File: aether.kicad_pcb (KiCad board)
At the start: 4 copper layers, 100.1 x 60.2 mm, 175 parts, among them J1 XT30PW-M, J2 Screw_Terminal_01x04, Q1 NPN, Q2 CSD17575Q3, Q3 CSD17575Q3, Q4 CSD17575Q3, Q5 CSD17575Q3, Q6 PNP, U1 USBLC6-2SC6, U10 TPS562201DDCR, U11 TPS562201DDCR, U12 INA219AxD, U2 USBLC6-2SC6, U3 SAM-M10Q-00B, U4 DPS310, U5 H3LIS331DL, U6 LSM6DSO32TR, U7 PCA9685PW, U8 MS860702BA01-50, U9 SHT45-AD1B-R2

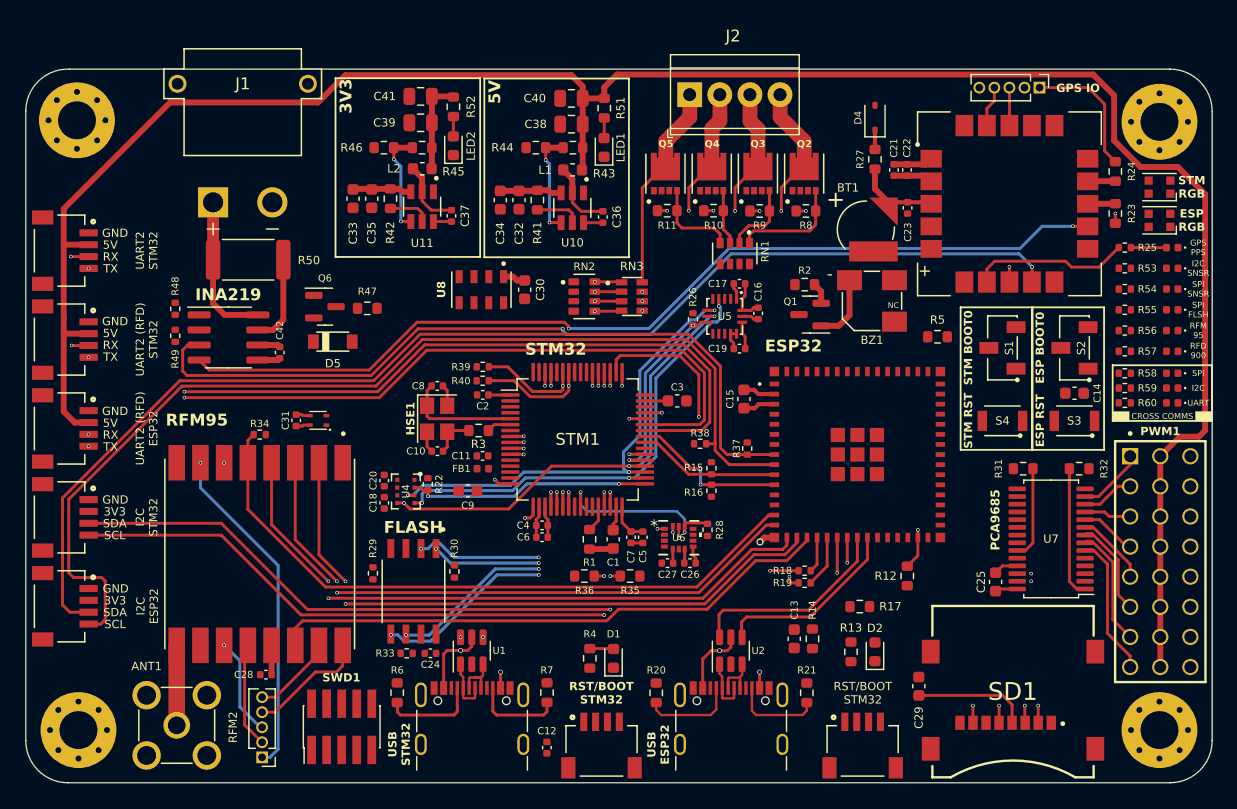
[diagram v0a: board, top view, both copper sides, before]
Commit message: signals routed
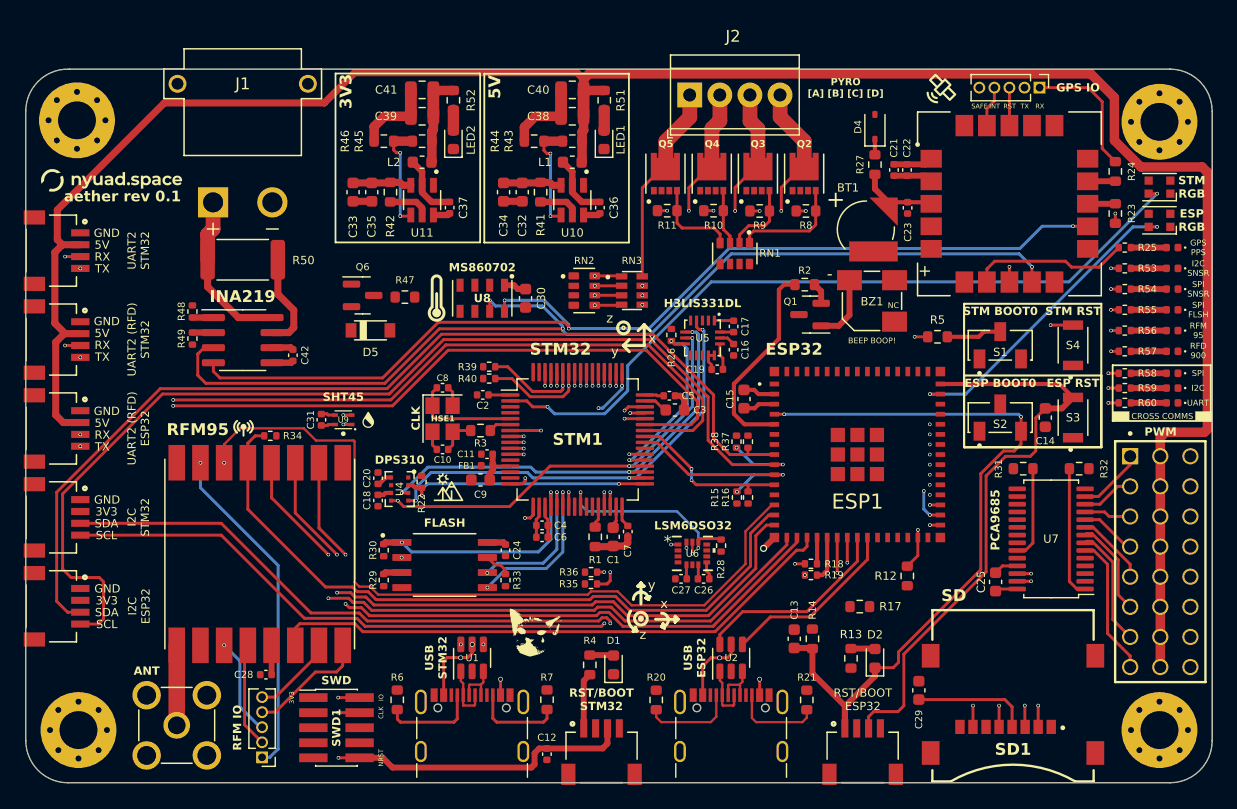
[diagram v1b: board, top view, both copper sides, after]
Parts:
- added G***: LOGO, LOGO, F.Cu at (133.9, 104.3)
- added G***: LOGO, LOGO, F.Cu at (116.6, 99.3)
- added G***: LOGO, LOGO, F.Cu at (127.1, 98.7)
- added G***: LOGO, LOGO, F.Cu at (141.0, 116.5)
- added G***: LOGO, LOGO, F.Cu at (175.5, 70.7)
- added G***: LOGO, LOGO, F.Cu at (105.4, 78.4)
- added G***: LOGO, LOGO, F.Cu at (132.9, 88.4)
- R35, R36: footprint Resistor_SMD:R_0603_1608Metric -> Resistor_SMD:R_0402_1005Metric
- moved C5 12.1 mm to (152.5, 96.6), turned to 0 degrees
- moved C24 10.8 mm to (138.7, 109.6), turned to -90 degrees
- moved R33 10.4 mm to (138.7, 112.2), turned to 90 degrees
- moved S4 8.72 mm to (186.6, 92.3), turned to 90 degrees
- moved S2 8.59 mm to (180.4, 98.4), turned to 0 degrees
- moved R30 6.23 mm to (128.4, 109.6)
- moved C16 3.70 mm to (157.9, 92.7), turned to -90 degrees
- moved C17 3.63 mm to (157.9, 90.8), turned to -90 degrees
- moved W25Q1 3.44 mm to (133.6, 110.9), turned to 0 degrees
- moved R35 3.36 mm to (145.9, 112.5), turned to 180 degrees
- moved D5 3.31 mm to (127.3, 91.1)
- moved Q6 3.31 mm to (126.7, 88.1)
- moved R47 3.31 mm to (130.2, 88.3)
- moved R15 3.27 mm to (158.2, 105.2), turned to -90 degrees
- moved C14 3.21 mm to (184.2, 98.4), turned to -90 degrees
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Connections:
- ESP1 pad 44: unconnected-(ESP1-IO46-Pad44) -> ESP32-RGB_IN
- RST-BOOT-ESP1 pad 2: GND -> 3.3V
- STM1 pad 2: unconnected-(STM1-PC13-Pad2) -> STM32-RGB_IN
- SWD1 pad 7: unconnected-(SWD1-Pin_7-Pad7) -> GND
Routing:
- net STM32-NRST: track 0.00 -> 119.3 mm, vias 0 -> 3
- net RFM95W_RST: track 0.00 -> 67.0 mm
- net STM32-RGB_IN: track 0.00 -> 64.7 mm, vias 0 -> 2
- net ESP32-GPIO0: track 0.05 -> 64.2 mm, vias 0 -> 2
- net GPS_SCL: track 94.8 -> 152.2 mm, vias 4 -> 6
- net GPS_SDA: track 95.1 -> 147.4 mm, vias 4 -> 6
- net ESP32-EN: track 0.01 -> 50.0 mm
- net STM32-BOOT0: track 0.02 -> 42.9 mm, vias 0 -> 2
- net STM32-SWCLK: track 1.15 -> 42.1 mm, vias 1 -> 3
- net STM32-SWDIO: track 0.00 -> 39.7 mm, vias 0 -> 2
- net ESP32-SPI2_MOSI: track 0.00 -> 37.7 mm, vias 0 -> 2
- net ESP32-SPI2_SCK: track 0.00 -> 36.5 mm, vias 0 -> 3
- net ESP32-SPI2_MISO: track 0.00 -> 35.8 mm, vias 0 -> 2
- net ESP32-RGB_IN: track 0.00 -> 26.6 mm, vias 0 -> 2
- net I2C-1_STM32: track 0.00 -> 21.6 mm, vias 0 -> 2
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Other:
- board text added: "ANT"
- board text added: "BEEP BOOP!"
- board text added: "CLK"
- board text added: "DPS310"
- board text added: "H3LIS331DL"
- board text added: "INT"
- board text added: "IO"
- board text added: "LSM6DSO32"
- board text added: "MS860702"
- board text added: "NRST"
- board text added: "PWM"
- board text added: "PYRO [A] [B] [C] [D]"
- board text added: "REF**"
- board text added: "RFM IO"
- board text added: "RST"
- board text added: "RST/BOOT ESP32"
- board text added: "SAFE"
- board text added: "SD"
- board text added: "SHT45"
- board text added: "SWD"
- board text added: "aether rev 0.1"
- board text added: "x"
- board text added: "y"
- board text added: "z"
